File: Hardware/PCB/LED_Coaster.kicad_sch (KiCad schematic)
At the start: 67 parts, among them J1 Li-po, J3 USB_C_Receptacle_USB2.0_16P, J4 UART, SW1 SW_SPDT, U1 ESP32-C3-WROOM-02-H4, U3 MCP73831-2-OT, U4 AMS1117-3.3

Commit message: Rework charging + power path: MCP73871, TLV75533, P-FET load switch
Schematic-side rework of the power section. The PCB still needs
"Update PCB from Schematic" (F8) plus placement/routing - see below.

Root causes fixed
- U3 (MCP73831) pin 2 V_SS sat on an isolated net shared only with R2 and
  never reached GND, so the charger never charged. The part is replaced
  outright and VSS (10, 11, EP) now ties to GND.
- U4 (AMS1117-3.3) needs ~1.3 V dropout; on battery it fell under the
  ESP32-C3 brown-out threshold. Replaced with a 238 mV-dropout LDO.
- LEDs and charger shared one +BATT node through a diode-OR, so LED current
  corrupted charge termination. The new charger has a real SYS power-path
  output, so system load and battery are separate.
- SW1 (JS102011SAQN, 300 mA) carried the full ~1.8 A LED rail. It is now a
  logic-level gate control; a P-FET carries the current.

Part swaps
- U3  MCP73831-2-OT SOT-23-5  -> MCP73871-2CC QFN-20-1EP 4x4 (LCSC C637761)
      footprint uses the _ThermalVias variant for EP stitching
- U4  AMS1117-3.3 SOT-223     -> TLV75533PDBVR SOT-23-5 (LCSC C404027)
- Q1  new AO3401A SOT-23 P-FET high-side load switch (LCSC C15127)
- D31, D32 (SS34 diode-OR) removed - the MCP73871 does this internally
- C4 2.2uF -> 4.7uF (datasheet requires >=4.7uF on OUT)
- R13 100k gate pull-up, R14 10k THERM, R15 20k PROG3, R16 1k + D35 for STAT2
- C8..C19 12x 100nF 0603 LED decoupling, C20 220uF bulk on the LED rail

Net changes
- +BATT  now only J1 <-> U3 VBAT/VBAT_SENSE and C7. Nothing else.
- +SYS   new. U3 OUT -> U4 input, Q1 source, R13. Must never merge with +BATT.
- +LED_PWR new. Q1 drain -> all 30 WS2812B VDD (was +BATT), C20 and C8..C19.
- GATE   local. Q1 gate, R13, SW1 pin C. SW1 pin B to GND, pin A unused.

Values from the MCP73871 datasheet (DS22090B)
- I_REG  = 1000 / R2  = 1000 / 2k  = 500 mA  (R2 keeps its 2k value)
- I_TERM = 1000 / R15 = 1000 / 20k = 50 mA
- THERM with no thermistor fitted: 10k to VSS (section 5.1.4)
- SEL low + PROG2 h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
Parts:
- removed D31, D32: SS34, Diode_SMD:D_SMA, symbol Diode:SS34
- removed U3: MCP73831-2-OT, Package_TO_SOT_SMD:SOT-23-5, symbol Battery_Management:MCP73831-2-OT
- removed U4: AMS1117-3.3, Package_TO_SOT_SMD:SOT-223-3_TabPin2, symbol Regulator_Linear:AMS1117-3.3
- added C10, C11, C12, C13, C14, C15, C16, C17, C18, C19, C8, C9: 100nF, Capacitor_SMD:C_0603_1608Metric_Pad1.08x0.95mm_HandSolder, symbol Device:C_Small
- added C20: 220uF, Capacitor_SMD:C_Elec_6.3x7.7, symbol Device:C_Small
- added D35: LED, LED_SMD:LED_0805_2012Metric_Pad1.15x1.40mm_HandSolder, symbol Device:LED
- added Q1: AO3401A, Package_TO_SOT_SMD:SOT-23, symbol Transistor_FET:AO3401A
- added R13: 100k, Resistor_SMD:R_0805_2012Metric_Pad1.20x1.40mm_HandSolder, symbol Device:R_Small
- added R14: 10k, Resistor_SMD:R_0805_2012Metric_Pad1.20x1.40mm_HandSolder, symbol Device:R_Small
- added R15: 20k, Resistor_SMD:R_0805_2012Metric_Pad1.20x1.40mm_HandSolder, symbol Device:R_Small
- added R16: 1k, Resistor_SMD:R_0805_2012Metric_Pad1.20x1.40mm_HandSolder, symbol Device:R_Small
- added U3: MCP73871-2CC, Package_DFN_QFN:QFN-20-1EP_4x4mm_P0.5mm_EP2.5x2.5mm_ThermalVias, symbol Battery_Management:MCP73871-2CC
- added U4: TLV75533PDBVR, Package_TO_SOT_SMD:SOT-23-5, symbol Regulator_Linear:TLV75533PDBV
- C4: value 2.2uF -> 4.7uF; MPN C377773 -> C1779
- J1: now fitted
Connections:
- net +3V3: now also C5.1, U4.5 (OUT); no longer C5.2
- net +5V: now also C6.1, D35.2 (A), U3.18 (IN), U3.19 (IN), U3.2 (VPCC); no longer C6.2
- net +BATT: now also C7.1, J1.2 (Pin_2), U3.14 (V_{BAT}), U3.15 (V_{BAT}), U3.16 (V_{BAT_SENSE}); no longer C4.2, D1.1 (VDD), D10.1 (VDD), D11.1 (VDD), D12.1 (VDD), D13.1 (VDD), D14.1 (VDD), D15.1 (VDD), D16.1 (VDD), D17.1 (VDD), D18.1 (VDD), D19.1 (VDD), D2.1 (VDD), D20.1 (VDD), D21.1 (VDD), D22.1 (VDD), D23.1 (VDD), D24.1 (VDD), D25.1 (VDD), D26.1 (VDD), D27.1 (VDD), D28.1 (VDD), D29.1 (VDD), D3.1 (VDD), D30.1 (VDD), D4.1 (VDD), D5.1 (VDD), D6.1 (VDD), D7.1 (VDD), D8.1 (VDD), D9.1 (VDD), SW1.3 (C)
- net GND: now also C4.2, C5.2, C6.2, C7.2, R2.2, SW1.2 (B), C10.2, C11.2, C12.2, C13.2, C14.2, C15.2, C16.2, C17.2, C18.2, C19.2, C20.2, C8.2, C9.2, R14.2, R15.2, U3.10 (V_{SS}), U3.11 (V_{SS}), U3.21 (V_{SS}), U3.3 (SEL), U4.2 (GND); no longer C4.1, C5.1, C6.1, C7.1
- net at R5.1: now also U3.8 (STAT1/~{LBO}); no longer D33.1 (K)
- net at R5.2: now also D33.1 (K)
- net at R2.1: now also U3.13 (PROG1)
- new net: R15.1, U3.12 (PROG3)
- new net: R14.1, U3.5 (THERM)
- new net: R16.1, U3.7 (STAT2)
- new net: Q1.1 (G), R13.1, SW1.3 (C)
- new net: D35.1 (K), R16.2
- new net +LED_PWR: C10.1, C11.1, C12.1, C13.1, C14.1, C15.1, C16.1, C17.1, C18.1, C19.1, C20.1, C8.1, C9.1, D1.1 (VDD), D10.1 (VDD), D11.1 (VDD), D12.1 (VDD), D13.1 (VDD), D14.1 (VDD), D15.1 (VDD), D16.1 (VDD), D17.1 (VDD), D18.1 (VDD), D19.1 (VDD), D2.1 (VDD), D20.1 (VDD), D21.1 (VDD), D22.1 (VDD), D23.1 (VDD), D24.1 (VDD), D25.1 (VDD), D26.1 (VDD), D27.1 (VDD), D28.1 (VDD), D29.1 (VDD), D3.1 (VDD), D30.1 (VDD), D4.1 (VDD), D5.1 (VDD), D6.1 (VDD), D7.1 (VDD), D8.1 (VDD), D9.1 (VDD), Q1.3 (D)
- new net +SYS: C4.1, Q1.2 (S), R13.2, U3.1 (OUT), U3.17 (CE), U3.20 (OUT), U3.4 (PROG2), U3.9 (~{TE}), U4.1 (IN), U4.3 (EN)
- no-connect marks 9 -> 10
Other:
- note added: "3V3 LDO"
- note added: "CE/TE/PROG2 strapped to SYS so they never float"
- note added: "LED power switch"
- note added: "LED ring decoupling - place one cap next to every 2-3 WS2812B on the PCB"
- note added: "Li-Po charger + power path"
- note added: "ON/OFF (logic level only)"
- note added: "STAT1 / STAT2"
- note added: "SYS output feeds LDO and LED switch - NOT the same net as BAT"
- note added: "charge current 1000/R2 = 500 mA"
- note added: "no NTC fitted: 10k to VSS"
- note added: "termination 1000/R15 = 50 mA"
- note removed: "LDO"
- note removed: "Li-Po charger"
- note removed: "ON/OFF"

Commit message: Restore true power-off and add battery-level sensing
Two follow-ups to the power-path rework.

1. SW1 is a real power switch again

The previous commit fed the LDO from +SYS, which is unswitched, so SW1 only
turned the LEDs off and the ESP32 stayed powered from the cell forever.
U4's EN pin now follows +LED_PWR instead, so flipping SW1 off collapses the
LED rail, which disables the LDO, which powers down the ESP32. Off-state
drain is then dominated by the MCP73871's own ~30 uA quiescent current.

The LDO *input* deliberately stays on the clean, unswitched +SYS node rather
than moving downstream of the FET, so LED load current never modulates the
MCU supply. R17 100k pulls +LED_PWR down to guarantee EN reaches 0 V even
with the LED array depopulated; with the LEDs fitted their ~30 mA quiescent
draw collapses the rail in milliseconds anyway.

Charging still works with the switch off - the charger's IN->BAT path is
independent of its SYS output - and the STAT LEDs run from +5V, so charge
state is still visible.

2. Battery level on GPIO4

R18/R19 470k divider from +BATT to a new BAT_SENSE net, buffered by C21
100nF, into U1 GPIO4 (ADC1_CH4, verified free and not a strapping pin).
Divide-by-2 puts the 3.0-4.2 V cell at 1.5-2.1 V, inside ADC1's linear range
on 12 dB attenuation. 470k costs ~4.5 uA of continuous draw, small against
the charger's own quiescent current; the 100nF supplies the SAR sampling
charge so the 235k source impedance is not a problem.

Nothing reads this yet. CLAUDE.md now carries a TODO covering the firmware
ADC work, the BLE contract change needed to report it, and the app side.

Co-Authored-By: Claude Opus 5 <noreply@anthropic.com>
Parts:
- added C21: 100nF, Capacitor_SMD:C_0805_2012Metric_Pad1.18x1.45mm_HandSolder, symbol Device:C_Small
- added R17: 100k, Resistor_SMD:R_0805_2012Metric_Pad1.20x1.40mm_HandSolder, symbol Device:R_Small
- added R18, R19: 470k, Resistor_SMD:R_0805_2012Metric_Pad1.20x1.40mm_HandSolder, symbol Device:R_Small
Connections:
- net +BATT: now also R18.1
- net +LED_PWR: now also U4.3 (EN), R17.1
- net +SYS: no longer U4.3 (EN)
- net GND: now also C21.2, R17.2, R19.2
- net BAT_SENSE: now reaches U1.3 (IO4)
- net BAT_SENSE: now also C21.1, R18.2, R19.1
- no-connect marks 10 -> 9
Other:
- note added: "LDO EN follows the LED rail so SW1 kills the whole board"
- note added: "battery sense -> GPIO4 (ADC1_CH4), divide by 2"

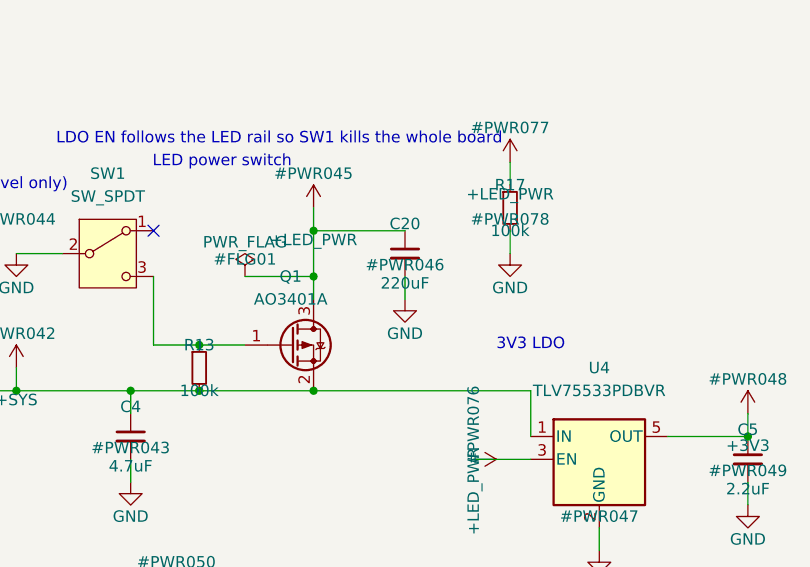
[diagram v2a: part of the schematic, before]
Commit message: Add PCB layout / JLCPCB ordering checklist; C20 to low-profile MLCC
ORDERING.md is a phase-by-phase checklist from installing KiCad through to
placing the order, with the placement, trace-width and DRC values specific to
this board rather than generic advice. CLAUDE.md points at it.

C20 changed from 220uF C_Elec_6.3x7.7 to 100uF 1210 MLCC:

- the electrolytic is 7.7 mm tall, which is wrong for a coaster
- it is polarized but was drawn on a non-polarized Device:C_Small symbol, so
  the silkscreen and pick-and-place rotation would not have shown polarity - a
  latent assembly hazard
- an MLCC has lower ESR for the LED transients the cap is there to absorb

Ceramics derate hard with DC bias, so 100uF nominal is more like 40-60 uF at
3.7 V. That is still a large improvement over the 2.2 uF the LED rail had
before, and a second cap can be paralleled if droop shows up.

Co-Authored-By: Claude Opus 5 <noreply@anthropic.com>
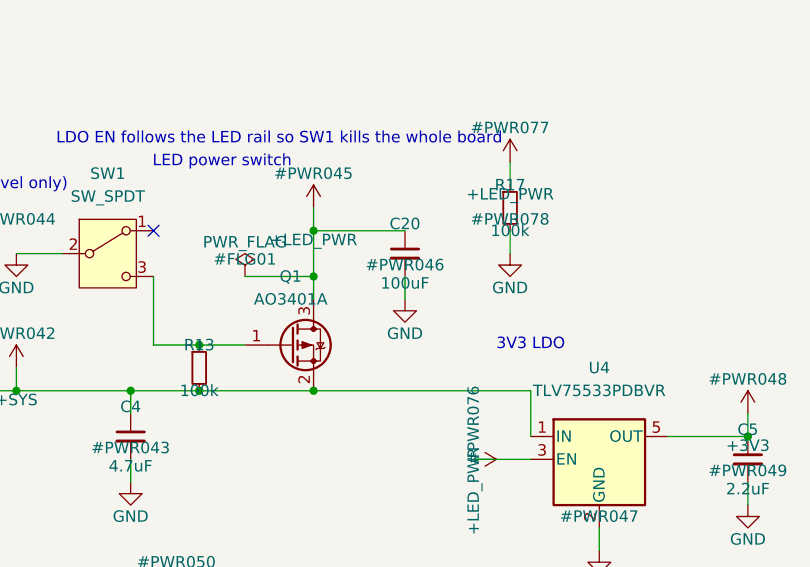
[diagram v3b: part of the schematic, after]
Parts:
- C20: value 220uF -> 100uF; footprint Capacitor_SMD:C_Elec_6.3x7.7 -> Capacitor_SMD:C_1210_3225Metric_Pad1.33x2.70mm_HandSolder
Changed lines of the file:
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@@
 			)
 		)
-		(property "Value" "220uF"
+		(property "Value" "100uF"
 			(at 500.38 212.852 0)
 			(effects
@@
 			)
 		)
-		(property "Footprint" "Capacitor_SMD:C_Elec_6.3x7.7"
+		(property "Footprint" "Capacitor_SMD:C_1210_3225Metric_Pad1.33x2.70mm_HandSolder"
 			(at 500.38 209.55 0)
 			(effects
